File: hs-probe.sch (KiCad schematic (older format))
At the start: 41 parts, among them J1 USB_C_Receptacle_USB2.0, U1 STM32F723IEKx, U2 DSC6003HI2A-012.0000T, U3 MIC5259-3.3YD5-TR, U4 NUF8401MNT4G, U5 STDC14, U6 SOICbite_SWD

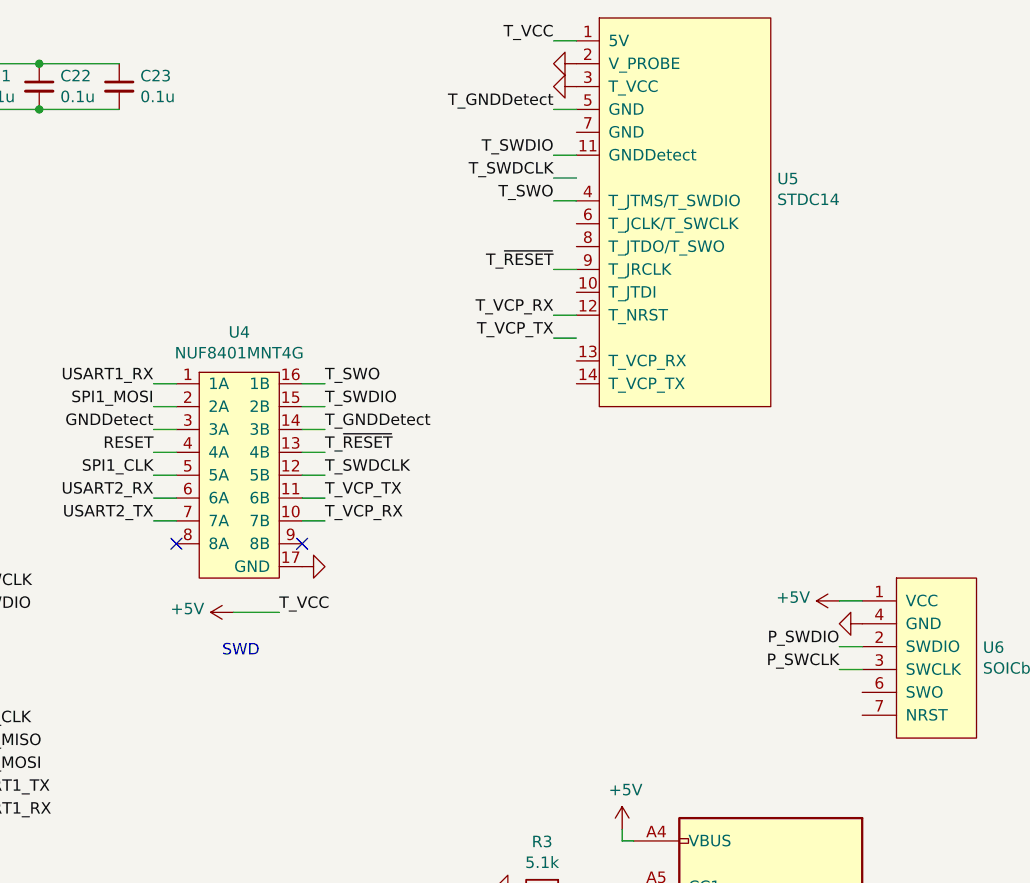
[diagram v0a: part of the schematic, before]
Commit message: Fixes on STDC14 connector, fixed component courtyards
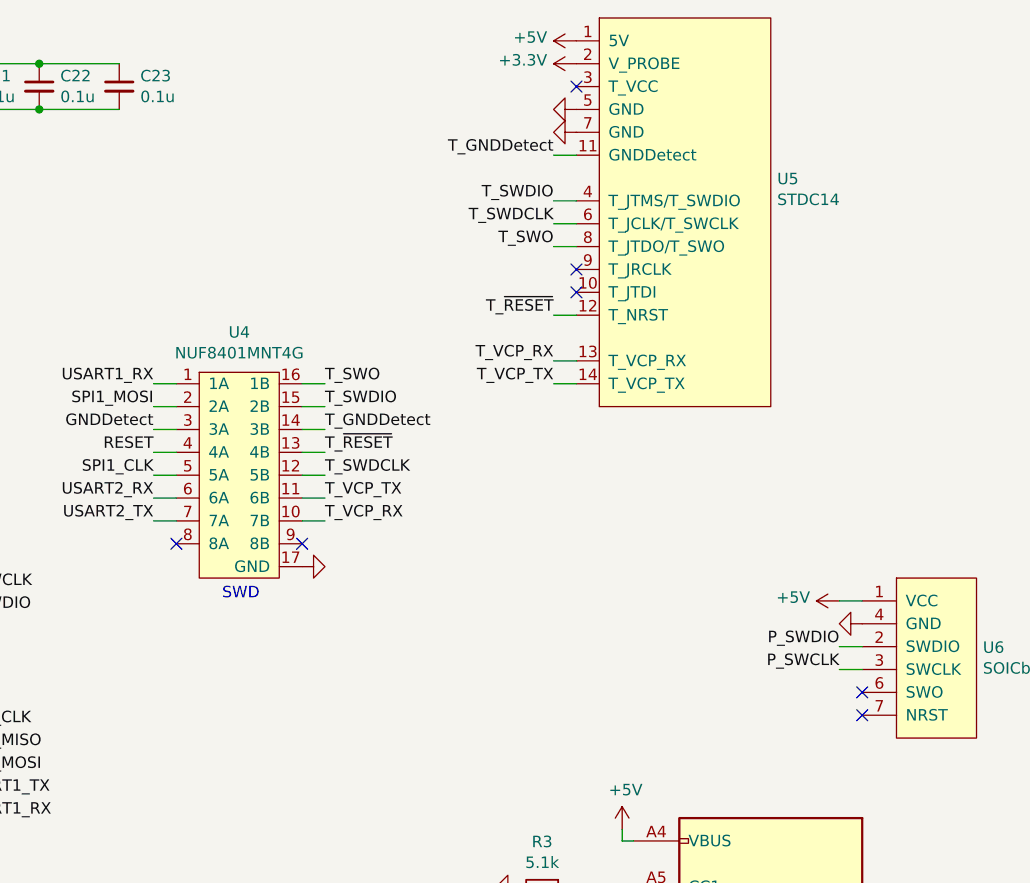
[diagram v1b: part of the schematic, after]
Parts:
- U1: footprint Package_BGA:UFBGA-201_10x10mm_Layout15x15_P0.65mm -> bga:UFBGA-201_10x10mm_Layout15x15_P0.65mm
- U5: footprint Connector_PinHeader_1.27mm:PinHeader_2x07_P1.27mm_Vertical_SMD -> connectors:PinHeader_2x07_P1.27mm_Vertical_SMD
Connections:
- net labels removed: T_VCC
- wire segments 176 -> 174
- no-connect marks 5 -> 10
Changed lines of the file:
@@
 F 0 "U1" H 8000 10431 50  0000 C CNN
 F 1 "STM32F723IEKx" H 8000 10340 50  0000 C CNN
-F 2 "Package_BGA:UFBGA-201_10x10mm_Layout15x15_P0.65mm" H 5750 1550 50  0001 R CNN
+F 2 "bga:UFBGA-201_10x10mm_Layout15x15_P0.65mm" H 5750 1550 50  0001 R CNN
 F 3 "http://www.st.com/st-web-ui/static/active/en/resource/technical/document/datasheet/DM00330506.pdf" H 8050 5850 50  0001 C CNN
 	1    8050 5850
@@
 Text Label 12150 2450 0    50   ~ 0
 T_GNDDetect
-Text Label 11950 3250 0    50   ~ 0
-T_VCC
-Text Notes 11700 3450 0    50   ~ 0
+Text Notes 11700 3200 0    50   ~ 0
 SWD
 Text Label 5450 8150 2    50   ~ 0
@@
 L power:+5V #PWR019
 U 1 1 5EA4368B
-P 11750 3250
-F 0 "#PWR019" H 11750 3100 50  0001 C CNN
-F 1 "+5V" V 11765 3378 50  0000 L CNN
-F 2 "" H 11750 3250 50  0001 C CNN
-F 3 "" H 11750 3250 50  0001 C CNN
-	1    11750 3250
+P 13250 750
+F 0 "#PWR019" H 13250 600 50  0001 C CNN
+F 1 "+5V" V 13265 878 50  0000 L CNN
+F 2 "" H 13250 750 50  0001 C CNN
+F 3 "" H 13250 750 50  0001 C CNN
+	1    13250 750
 	0    -1   -1   0
 $EndComp
-Wire Wire Line
-	11750 3250 11950 3250
 $Comp
 L Regulator_Linear:MIC5504-3.3YM5 U3
@@
 F 0 "U5" H 14128 -54 50  0000 L CNN
 F 1 "STDC14" H 14128 -145 50  0000 L CNN
-F 2 "Connector_PinHeader_1.27mm:PinHeader_2x07_P1.27mm_Vertical_SMD" H 13350 650 50  0001 C CNN
+F 2 "connectors:PinHeader_2x07_P1.27mm_Vertical_SMD" H 13350 650 50  0001 C CNN
 F 3 "" H 13350 650 50  0001 C CNN
 	1    13350 650
@@
 $EndComp
 Wire Wire Line
-	13250 1250 13150 1250
-Wire Wire Line
-	13250 1350 13150 1350
-Wire Wire Line
 	13250 1450 13150 1450
 Wire Wire Line
-	13250 1750 13150 1750
-Wire Wire Line
-	13150 1050 13250 1050
-Wire Wire Line
-	13150 750  13250 750
-Text Label 13150 1750 2    50   ~ 0
+	13250 1550 13150 1550
+Wire Wire Line
+	13250 1650 13150 1650
+Wire Wire Line
+	13250 1950 13150 1950
+Wire Wire Line
+	13150 1250 13250 1250
+Text Label 13150 1950 2    50   ~ 0
 T_~RESET
+Text Label 13150 1650 2    50   ~ 0
+T_SWO
+Text Label 13150 1550 2    50   ~ 0
+T_SWDCLK
 Text Label 13150 1450 2    50   ~ 0
-T_SWO
-Text Label 13150 1350 2    50   ~ 0
-T_SWDCLK
+T_SWDIO
 Text Label 13150 1250 2    50   ~ 0
-T_SWDIO
-Text Label 13150 1050 2    50   ~ 0
 T_GNDDetect
 $Comp
 L power:GND #PWR030
 U 1 1 5EB7AA5C
-P 13250 950
-F 0 "#PWR030" H 13250 700 50  0001 C CNN
-F 1 "GND" H 13255 777 50  0001 C CNN
-F 2 "" H 13250 950 50  0001 C CNN
-F 3 "" H 13250 950 50  0001 C CNN
-	1    13250 950
+P 13250 1150
+F 0 "#PWR030" H 13250 900 50  0001 C CNN
+F 1 "GND" H 13255 977 50  0001 C CNN
+F 2 "" H 13250 1150 50  0001 C CNN
+F 3 "" H 13250 1150 50  0001 C CNN
+	1    13250 1150
 	0    1    1    0
 $EndComp
@@
 L power:GND #PWR023
 U 1 1 5EB7AA62
-P 13250 850
-F 0 "#PWR023" H 13250 600 50  0001 C CNN
-F 1 "GND" H 13255 677 50  0001 C CNN
-F 2 "" H 13250 850 50  0001 C CNN
-F 3 "" H 13250 850 50  0001 C CNN
-	1    13250 850
-	0    1    1    0
-$EndComp
-Text Label 13150 750  2    50   ~ 0
-T_VCC
+P 13250 1050
+F 0 "#PWR023" H 13250 800 50  0001 C CNN
+F 1 "GND" H 13255 877 50  0001 C CNN
+F 2 "" H 13250 1050 50  0001 C CNN
+F 3 "" H 13250 1050 50  0001 C CNN
+	1    13250 1050
+	0    1    1    0
+$EndComp
 $Comp
 L interface_esd:NUF8401MNT4G U4
@@
 Wire Wire Line
 	11400 2550 11500 2550
-Text Label 13150 1950 2    50   ~ 0
+Text Label 13150 2150 2    50   ~ 0
 T_VCP_RX
-Text Label 13150 2050 2    50   ~ 0
+Text Label 13150 2250 2    50   ~ 0
 T_VCP_TX
 Wire Wire Line
-	13150 1950 13250 1950
-Wire Wire Line
-	13150 2050 13250 2050
+	13150 2150 13250 2150
+Wire Wire Line
+	13150 2250 13250 2250
 Text Label 12150 2850 0    50   ~ 0
 T_VCP_RX
@@
 Wire Wire Line
 	10550 2850 10450 2850
+$Comp
+L power:+3.3V #PWR0103
+U 1 1 5E86FD7D
+P 13250 850
+F 0 "#PWR0103" H 13250 700 50  0001 C CNN
+F 1 "+3.3V" V 13265 978 50  0000 L CNN
+F 2 "" H 13250 850 50  0001 C CNN
+F 3 "" H 13250 850 50  0001 C CNN
+	1    13250 850
+	0    -1   -1   0
+$EndComp
+NoConn ~ 13250 950
+NoConn ~ 14500 3700
+NoConn ~ 14500 3600
+NoConn ~ 13250 1750
+NoConn ~ 13250 1850
 $EndSCHEMATC

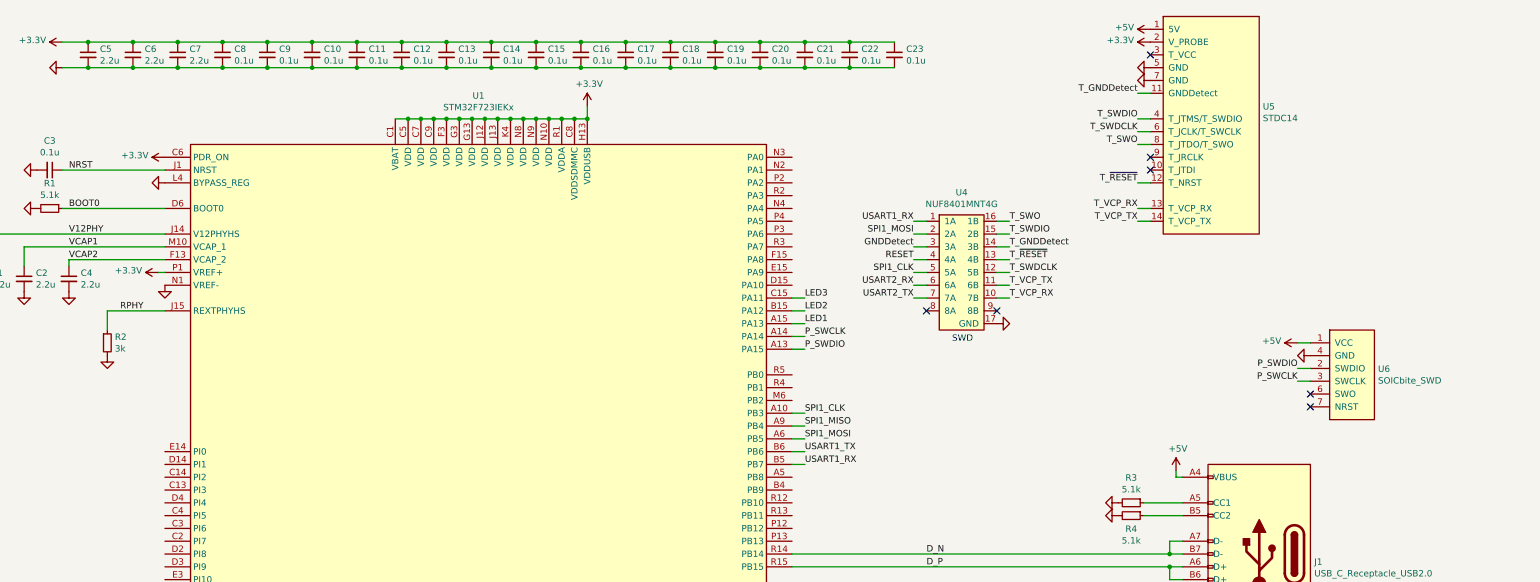
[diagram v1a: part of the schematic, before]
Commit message: Added JTAG on SPI2
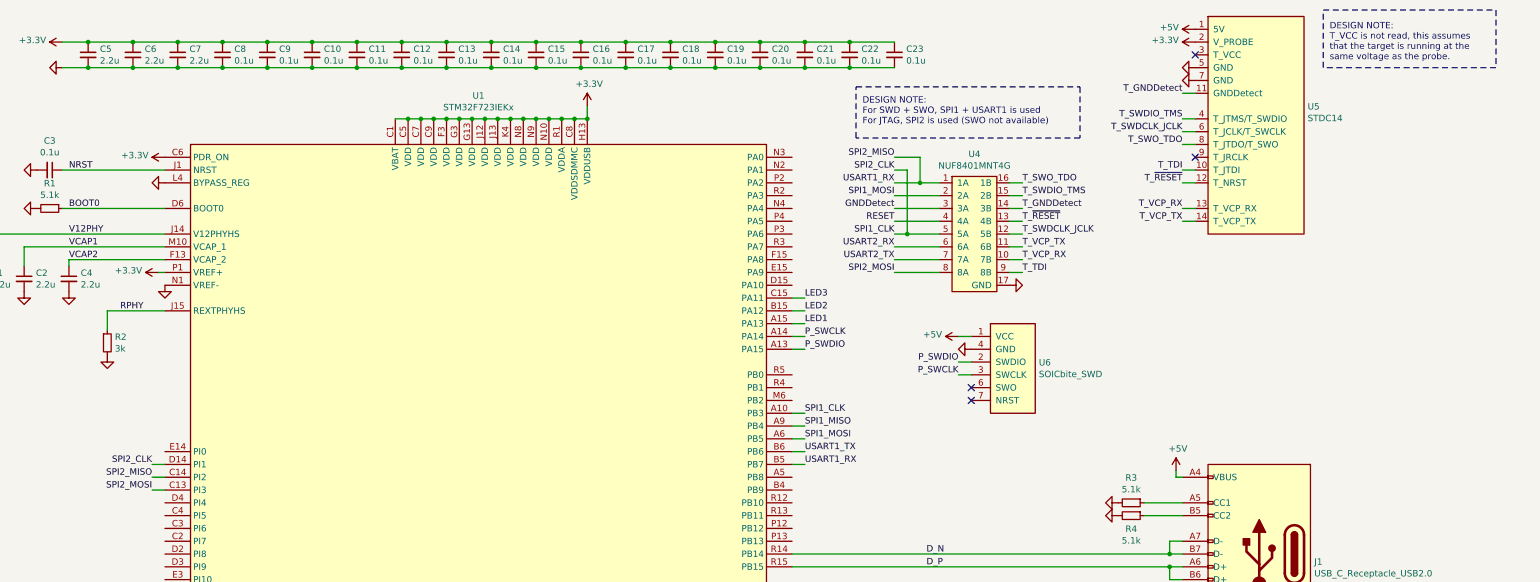
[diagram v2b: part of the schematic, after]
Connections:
- net labels added: SPI2_CLK, SPI2_MISO, SPI2_MOSI, T_SWDCLK_JCLK, T_SWDIO_TMS, T_SWO_TDO, T_TDI
- net labels removed: T_SWDCLK, T_SWDIO, T_SWO
- wire segments 174 -> 186
- no-connect marks 10 -> 7
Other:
- note added: "DESIGN NOTE:\nFor SWD + SWO, SPI1 + USART1 is used\nFor JTAG, SPI2 is used (SWO not available)"
- note added: "DESIGN NOTE:\nT_VCC is not read, this assumes\nthat the target is running at the\nsame voltage as the probe."
- note removed: "SWD"
- moved on the sheet: U4, U5, U6

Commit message: Minor updates
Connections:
- wire segments 186 -> 187
- no-connect marks 7 -> 6
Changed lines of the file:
@@
 Text Label 10550 2950 0    50   ~ 0
 LED2
-$Comp
-L connectors:SOICbite_SWD U6
-U 1 1 5EFB31C8
-P 12000 3050
-F 0 "U6" H 12378 2746 50  0000 L CNN
-F 1 "SOICbite_SWD" H 12378 2655 50  0000 L CNN
-F 2 "connectors:SOICbiteSmall" H 12000 3050 50  0001 C CNN
-F 3 "https://github.com/SimonMerrett/SOICbite" H 12000 3050 50  0001 C CNN
-	1    12000 3050
-	1    0    0    -1
-$EndComp
 Text Label 10550 3250 0    50   ~ 0
 P_SWDIO
@@
 $EndComp
 NoConn ~ 13600 950
-NoConn ~ 11850 3650
 NoConn ~ 11850 3550
 NoConn ~ 13600 1750
@@
 Wire Notes Line
 	14600 1050 14600 600
+Text Label 11750 3650 2    50   ~ 0
+NRST
+$Comp
+L connectors:SOICbite_SWD U6
+U 1 1 5EFB31C8
+P 12000 3050
+F 0 "U6" H 12378 2746 50  0000 L CNN
+F 1 "SOICbite_SWD" H 12378 2655 50  0000 L CNN
+F 2 "connectors:SOICbiteSmall" H 12000 3050 50  0001 C CNN
+F 3 "https://github.com/SimonMerrett/SOICbite" H 12000 3050 50  0001 C CNN
+	1    12000 3050
+	1    0    0    -1
+$EndComp
+Wire Wire Line
+	11750 3650 11850 3650
 $EndSCHEMATC

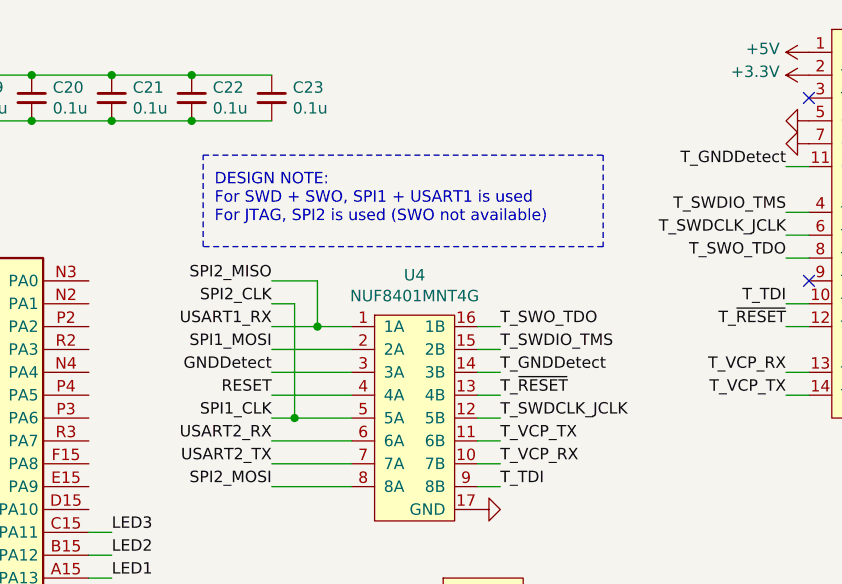
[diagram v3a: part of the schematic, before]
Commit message: Shorted SPI1 MISO/MOSI, rotated connector
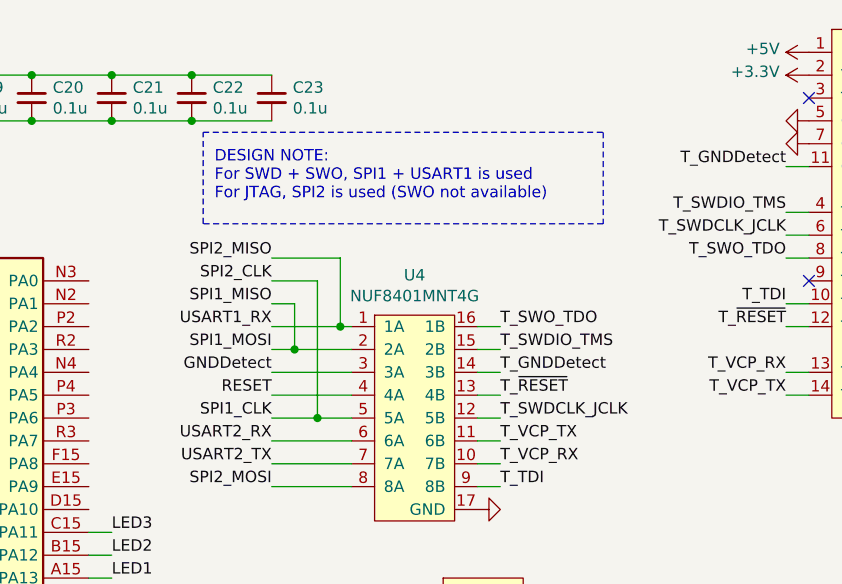
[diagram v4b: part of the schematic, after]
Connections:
- wire segments 187 -> 190
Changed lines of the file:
@@
 	12150 2250 12250 2250
 Wire Wire Line
-	11250 1950 11450 1950
-Wire Wire Line
-	11250 2050 11600 2050
+	11250 1950 11550 1950
+Wire Wire Line
+	11250 2050 11350 2050
 Wire Wire Line
 	11250 2150 11600 2150
@@
 Text Label 11250 2650 2    50   ~ 0
 SPI2_MOSI
+Text Label 11250 1650 2    50   ~ 0
+SPI2_MISO
 Text Label 11250 1750 2    50   ~ 0
-SPI2_MISO
-Text Label 11250 1850 2    50   ~ 0
 SPI2_CLK
 Wire Wire Line
@@
 Text Label 13500 1850 2    50   ~ 0
 T_TDI
-Text Notes 11000 1500 0    50   ~ 0
+Text Notes 11000 1400 0    50   ~ 0
 DESIGN NOTE:\nFor SWD + SWO, SPI1 + USART1 is used\nFor JTAG, SPI2 is used (SWO not available)
 Wire Wire Line
-	11250 2350 11350 2350
-Wire Wire Line
-	11250 1850 11350 1850
-Wire Wire Line
-	11350 1850 11350 2350
-Connection ~ 11350 2350
-Wire Wire Line
-	11350 2350 11600 2350
+	11250 2350 11450 2350
+Wire Wire Line
+	11250 1750 11450 1750
+Wire Wire Line
+	11450 1750 11450 2350
+Connection ~ 11450 2350
+Wire Wire Line
+	11450 2350 11600 2350
 Wire Wire Line
 	11250 2650 11600 2650
@@
 	12250 2650 12150 2650
 Wire Wire Line
-	11250 1750 11450 1750
-Wire Wire Line
-	11450 1750 11450 1950
-Connection ~ 11450 1950
-Wire Wire Line
-	11450 1950 11600 1950
-Wire Notes Line
-	10950 1200 12700 1200
-Wire Notes Line
-	12700 1200 12700 1600
-Wire Notes Line
-	12700 1600 10950 1600
-Wire Notes Line
-	10950 1600 10950 1200
+	11250 1650 11550 1650
+Wire Wire Line
+	11550 1650 11550 1950
+Connection ~ 11550 1950
+Wire Wire Line
+	11550 1950 11600 1950
+Wire Notes Line
+	10950 1100 12700 1100
+Wire Notes Line
+	12700 1100 12700 1500
+Wire Notes Line
+	12700 1500 10950 1500
+Wire Notes Line
+	10950 1500 10950 1100
 Text Notes 14650 1000 0    50   ~ 0
 DESIGN NOTE:\nT_VCC is not read, this assumes\nthat the target is running at the\nsame voltage as the probe.
@@
 Wire Wire Line
 	11750 3650 11850 3650
+Wire Wire Line
+	11250 1850 11350 1850
+Wire Wire Line
+	11350 1850 11350 2050
+Connection ~ 11350 2050
+Wire Wire Line
+	11350 2050 11600 2050
+Text Label 11250 1850 2    50   ~ 0
+SPI1_MISO
 $EndSCHEMATC

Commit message: Added ESD protection, fixed silkscreen
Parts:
- removed U3: MIC5259-3.3YD5-TR, sot:SOT-23-5, symbol Regulator_Linear:MIC5504-3.3YM5
- added C26, C27: 2.2u, passive:C_0402, symbol Device:C_Small
- added D2: ESD7002WTT1G, sot:SOT-323, symbol Device:D_Zener_x2_ACom_KKA
- added U3, U7: MIC5259, dfn:DFN-6-1EP_2x2mm_P0.65mm_EP1x1.6mm, symbol ldo:MIC5259
- C24, C25: value 4.7u -> 2.2u; footprint passive:C_0603 -> passive:C_0402
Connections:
- net labels added: T_VCC, T_VCC_EN
- wire segments 190 -> 208
- no-connect marks 6 -> 7

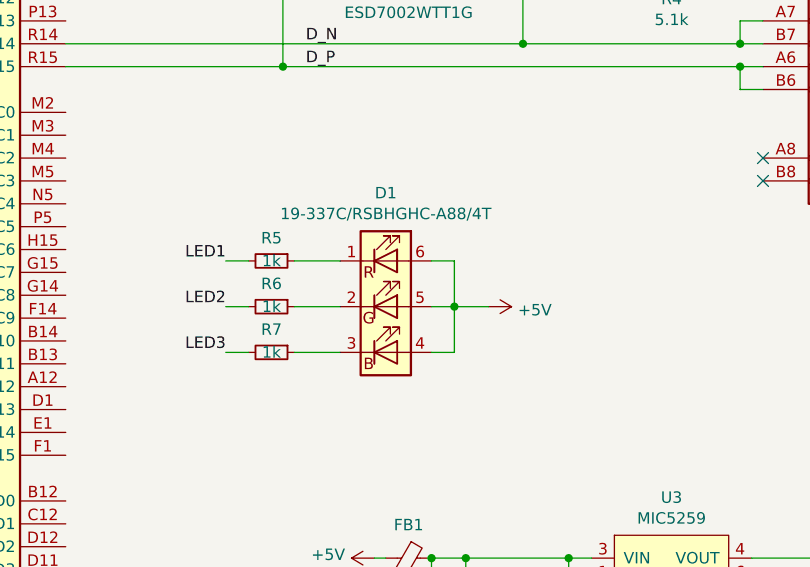
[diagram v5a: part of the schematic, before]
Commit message: Updated LED for a more commonly available one
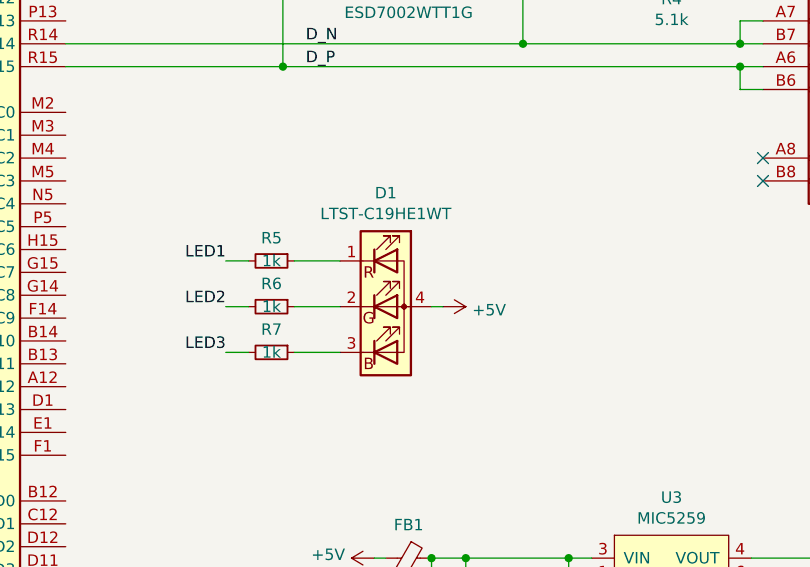
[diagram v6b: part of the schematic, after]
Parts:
- removed D1: 19-337C/RSBHGHC-A88/4T, leds:0606, symbol Device:LED_RGB
- added D1: LTST-C19HE1WT, LED_SMD:LED_LiteOn_LTST-C19HE1WT, symbol Device:LED_RGBA
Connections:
- net +5V: now also D1.4 (A)
- net at R5.1: now also D1.1 (RK)
- net at R6.1: now also D1.2 (GK)
- net at R7.1: now also D1.3 (BK)
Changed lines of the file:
@@
 USART2_TX
-$Comp
-L Device:LED_RGB D1
-U 1 1 5EF031E4
-P 11850 6000
-F 0 "D1" H 11850 6497 50  0000 C CNN
-F 1 "19-337C/RSBHGHC-A88/4T" H 11850 6406 50  0000 C CNN
-F 2 "leds:0606" H 11850 5950 50  0001 C CNN
-F 3 "https://media.digikey.com/pdf/Data%20Sheets/Everlight%20PDFs/19-337C_RSBHGHC-A88_4T_Rev2_1-25-19.pdf" H 11850 5950 50  0001 C CNN
-	1    11850 6000
-	1    0    0    -1
-$EndComp
 $Comp
 L Device:R_Small R5
@@
 L power:+5V #PWR031
 U 1 1 5EF2C3C5
-P 12300 6000
-F 0 "#PWR031" H 12300 5850 50  0001 C CNN
-F 1 "+5V" V 12315 6128 50  0000 L CNN
-F 2 "" H 12300 6000 50  0001 C CNN
-F 3 "" H 12300 6000 50  0001 C CNN
-	1    12300 6000
-	0    1    1    0
-$EndComp
-Wire Wire Line
-	12050 5800 12150 5800
-Wire Wire Line
-	12150 5800 12150 6000
-Wire Wire Line
-	12150 6200 12050 6200
-Wire Wire Line
-	12050 6000 12150 6000
-Connection ~ 12150 6000
-Wire Wire Line
-	12150 6000 12150 6200
-Wire Wire Line
-	12150 6000 12300 6000
+P 12100 6000
+F 0 "#PWR031" H 12100 5850 50  0001 C CNN
+F 1 "+5V" V 12115 6128 50  0000 L CNN
+F 2 "" H 12100 6000 50  0001 C CNN
+F 3 "" H 12100 6000 50  0001 C CNN
+	1    12100 6000
+	0    1    1    0
+$EndComp
 Text Label 11150 5800 2    50   ~ 0
 LED1
@@
 Wire Wire Line
 	11400 4950 13400 4950
+$Comp
+L Device:LED_RGBA D1
+U 1 1 5E8EC8DB
+P 11850 6000
+F 0 "D1" H 11850 6497 50  0000 C CNN
+F 1 "LTST-C19HE1WT" H 11850 6406 50  0000 C CNN
+F 2 "LED_SMD:LED_LiteOn_LTST-C19HE1WT" H 11850 5950 50  0001 C CNN
+F 3 "https://optoelectronics.liteon.com/upload/download/DS22-2008-0044/LTST-C19HE1WT.pdf" H 11850 5950 50  0001 C CNN
+	1    11850 6000
+	1    0    0    -1
+$EndComp
+Wire Wire Line
+	12050 6000 12100 6000
 $EndSCHEMATC
